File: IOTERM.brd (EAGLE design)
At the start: 135.9 x 53.3 mm, 45 parts

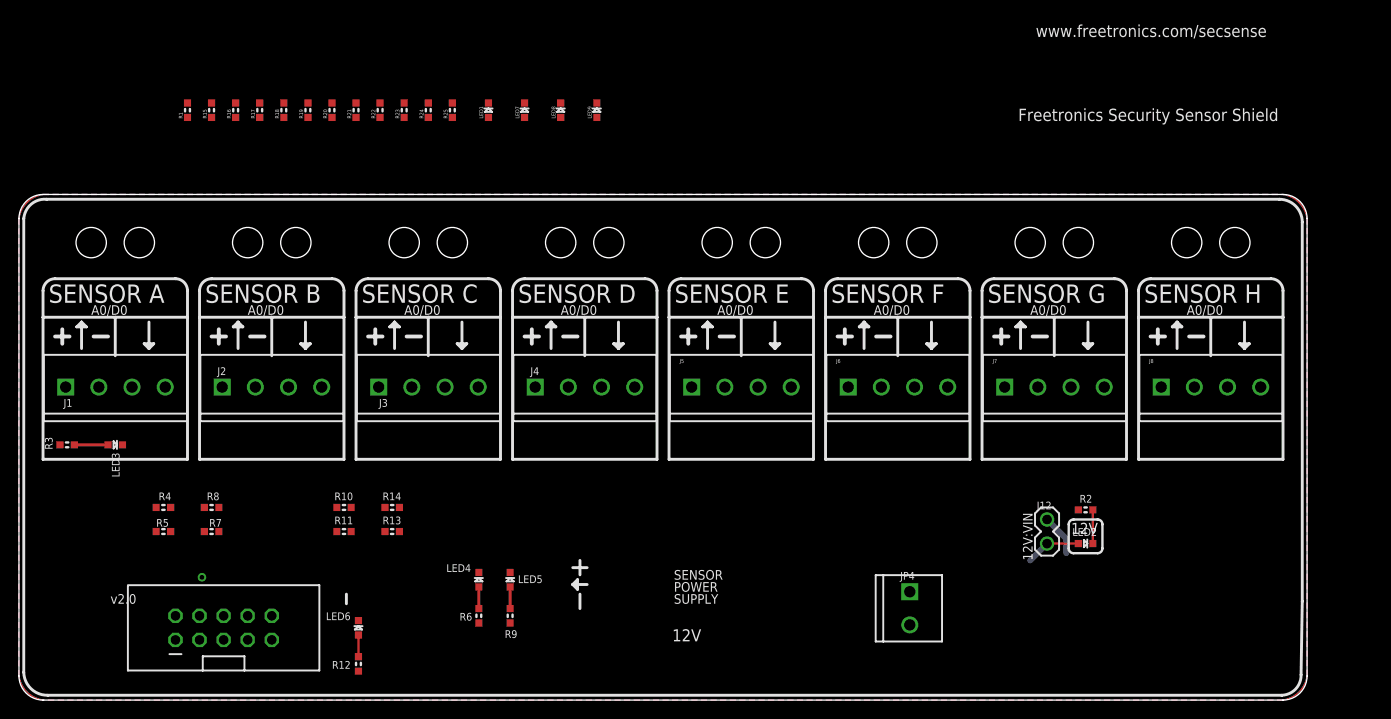
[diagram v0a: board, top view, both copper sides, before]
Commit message: Expanded header to 2x6 for v2.0 release
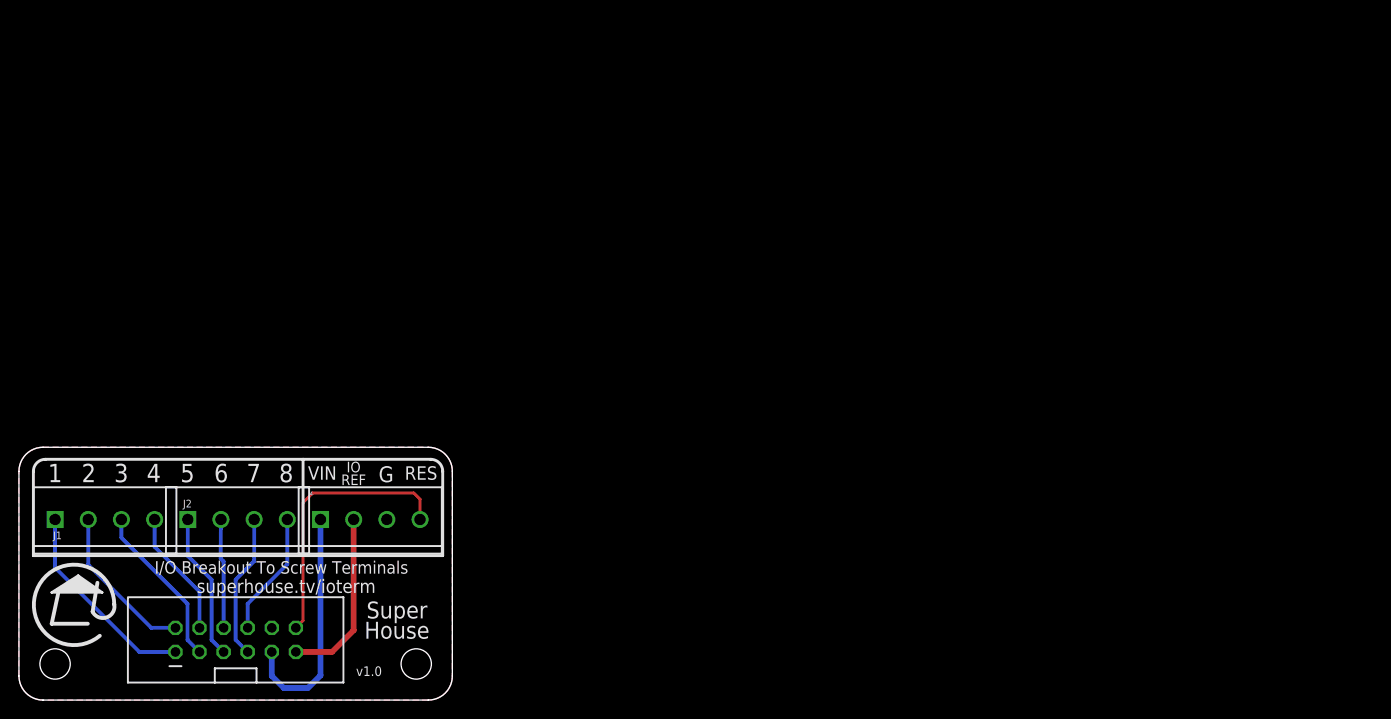
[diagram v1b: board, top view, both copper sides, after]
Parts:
- removed J12: (no value), freetronics-original:1X02
- removed J3, J5, J6, J7, J8: (no value), freetronics-master-v1.1:SCREWTERMINAL-3.5MM-4
- removed JP4: (no value), freetronics-master-v1.1:SCREWTERMINAL-3.5MM-2
- removed LED1, LED3, LED4, LED5, LED6, LED7, LED8, LED9: RED, freetronics-jon:LED-0603
- removed LED2: GREEN, freetronics-jon:LED-0603
- removed R1, R12, R15, R16, R17, R3, R6, R9: 560R, freetronics-jon:0603
- removed R10, R13, R18, R19, R20, R21, R4, R7: 4K7, freetronics-jon:0603
- removed R11, R14, R2, R22, R23, R24, R25, R5, R8: 1K, freetronics-jon:0603
- J1: value (none) -> D0_D3
- J2: value (none) -> D4_D7
- J4: value (none) -> Power
- JP1: value M05X2SHD -> M06X2; device freetronics-original:2X5-SHROUDED -> freetronics-jon:2X6-SHROUDED
- moved J4 26.6 mm to (31.8, 19.1)
- moved J2 14.4 mm to (17.8, 19.1)
- moved J1 14.0 mm to (3.81, 19.1)
- moved JP1 5.68 mm to (16.5, 5.08)
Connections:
- removed net 12V: J1.1, J12.1, J2.1, J3.1, J4.1, J5.1, J6.1, J7.1, J8.1, JP4.1, LED2.A
- removed net 5V: R10.1, R13.1, R18.1, R19.1, R20.1, R21.1, R4.1, R7.1
- removed net A0: R5.1
- removed net A1: R8.1
- removed net A2: R11.1
- removed net A3: R14.1
- removed net N$1: LED2.C, R2.2
- removed net N$10: J8.4, R21.2, R25.2
- removed net N$11: JP1.5
- removed net N$12: JP1.3
- removed net N$13: JP1.1
- removed net N$14: JP1.7
- removed net N$15: LED1.A, R1.1
- removed net N$16: LED7.A, R15.1
- removed net N$17: LED8.A, R16.1
- removed net N$18: LED9.A, R17.1
- removed net N$19: R1.2
- removed net N$2: R3.2
- removed net N$20: R15.2
- removed net N$21: R16.2
- removed net N$22: R17.2
- removed net N$23: R22.1
- removed net N$24: R23.1
- removed net N$249: J3.4, R10.2, R11.2
- removed net N$25: R24.1
- removed net N$251: LED6.A, R12.1
- removed net N$252: LED5.A, R9.1
- removed net N$253: LED4.A, R6.1
- removed net N$254: LED3.A, R3.1
- removed net N$256: J4.4, R13.2, R14.2
- removed net N$26: R25.1
- removed net N$262: J1.4, R4.2, R5.2
- removed net N$27: JP1.8
- removed net N$28: JP1.6
- removed net N$29: JP1.4
- removed net N$3: J2.4, R7.2, R8.2
- removed net N$30: JP1.2
- removed net N$4: R6.2
- removed net N$5: R9.2
- removed net N$6: R12.2
- removed net N$7: J5.4, R18.2, R22.2
- removed net N$8: J6.4, R19.2, R23.2
- removed net N$9: J7.4, R20.2, R24.2
- removed net VCC: JP1.9
- new net D0: J1.1, JP1.1
- new net D1: J1.2, JP1.2
- new net D2: J1.3, JP1.3
- new net D3: J1.4, JP1.4
- new net D4: J2.1, JP1.5
- new net D5: J2.2, JP1.6
- new net D6: J2.3, JP1.7
- new net D7: J2.4, JP1.8
- new net IOREF: J4.2, JP1.11
- new net RESET: J4.4, JP1.12
- net GND: no longer J1.2, J1.3, J2.2, J2.3, J3.2, J3.3, J4.2, J5.2, J5.3, J6.2, J6.3, J7.2, J7.3, J8.2, J8.3, JP4.2, LED1.C, LED3.C, LED4.C, LED5.C, LED6.C, LED7.C, LED8.C, LED9.C, R2.1
- net VIN: now also J4.1, JP1.9; no longer J12.2
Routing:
- net RESET: track 0.00 -> 28.7 mm
- net D0: track 0.00 -> 21.5 mm
- net VIN: track 4.40 -> 25.2 mm
- net IOREF: track 0.00 -> 18.7 mm
- net D2: track 0.00 -> 17.4 mm
- net D1: track 0.00 -> 16.7 mm
- net D4: track 0.00 -> 15.5 mm
- net D6: track 0.00 -> 15.3 mm
- net D3: track 0.00 -> 13.4 mm
- net D7: track 0.00 -> 13.2 mm
- net D5: track 0.00 -> 11.6 mm
- net 12V: track 5.82 -> 0.00 mm
- net N$254: track 3.56 -> 0.00 mm
- net N$1: track 3.56 -> 0.00 mm
- net N$253: track 2.29 -> 0.00 mm
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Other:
- board size 135.9 x 53.3 mm -> 45.7 x 26.7 mm
- board text added: "(c) 2017 SuperHouse Automation Pty Ltd"
- board text added: "1"
- board text added: "2"
- board text added: "3"
- board text added: "4"
- board text added: "5"
- board text added: "6"
- board text added: "7"
- board text added: "8"
- board text added: "G"
- board text added: "GND"
- board text added: "I/O Breakout To Screw Terminals"
- board text added: "IO REF"
- board text added: "IOREF"
- board text added: "RES"
- board text added: "RESET"
- board text added: "SKU: IOTERM"
- board text added: "Super House"
- board text added: "VIN"
- board text added: "superhouse.tv/ioterm"
- board text added: "v1.0"
- board text removed: "(c) 2013 Freetronics Pty Ltd"
- board text removed: "+12V"
- board text removed: "0V"
- board text removed: "12V"
- board text removed: "12V:VIN"
- board text removed: "4-Channel Security Sensor Shield"
- board text removed: "4K7"
- board text removed: "A"
- board text removed: "A0/D0"
- board text removed: "A: A0/D4 B: A1/D5 C: A2/D6 D: A3/D7"
- board text removed: "ALARM N.C."
- board text removed: "Freetronics Security Sensor Shield"
- board text removed: "K"
- board text removed: "POWER"
- board text removed: "SENSOR"
- board text removed: "SENSOR A"
- board text removed: "SENSOR B"
- board text removed: "SENSOR C"
- board text removed: "SENSOR D"
- board text removed: "SENSOR E"
- board text removed: "SENSOR F"
- board text removed: "SENSOR G"
- board text removed: "SENSOR H"
- board text removed: "SHIELD"
- board text removed: "SKU: SECSENSE"
- board text removed: "SUPPLY"
- board text removed: "TAMPER N.C."
- board text removed: "freetronics"
- board text removed: "v2.0"
- board text removed: "www.freetronics.com"
- board text removed: "www.freetronics.com/secsense"

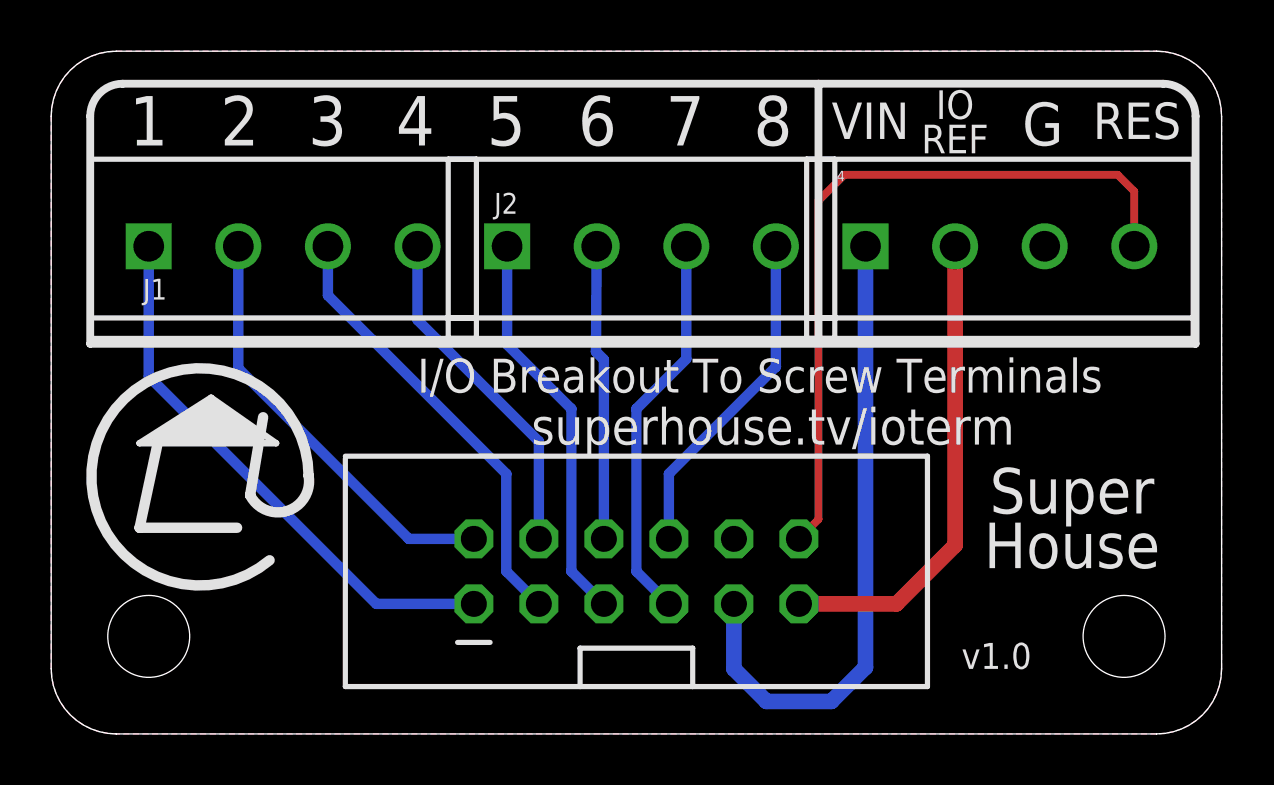
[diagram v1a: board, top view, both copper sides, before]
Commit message: Adjusted size to metric grid
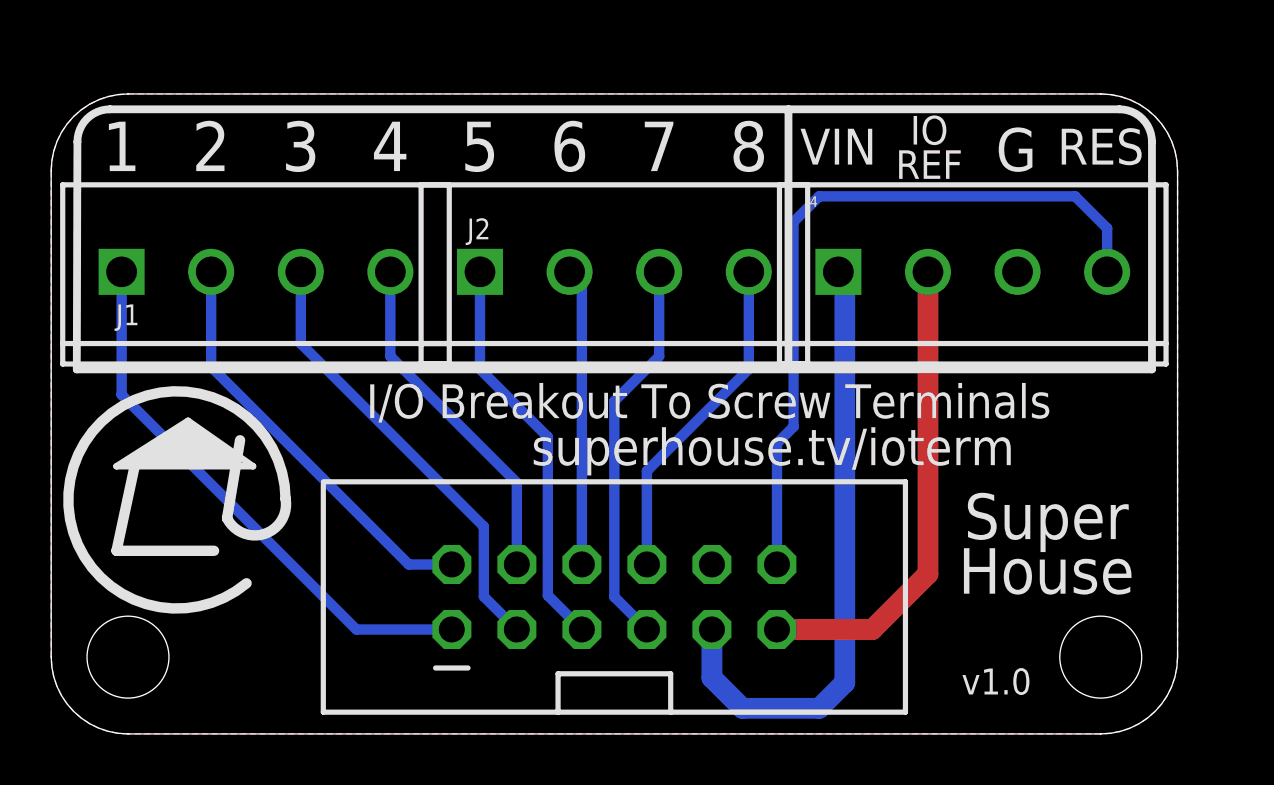
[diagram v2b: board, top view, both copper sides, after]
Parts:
- moved J1 1.46 mm to (2.75, 18.1)
- moved J2 1.46 mm to (16.8, 18.1)
- moved J4 1.46 mm to (30.8, 18.1)
- moved JP1 1.32 mm to (15.7, 4.08)
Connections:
- net D0 renamed IO1
- net D1 renamed IO2
- net D2 renamed IO3
- net D3 renamed IO4
- net D4 renamed IO5
- net D5 renamed IO6
- net D6 renamed IO7
- net D7 renamed IO8
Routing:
- net VIN: track 25.2 -> 24.1 mm
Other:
- board size 45.7 x 26.7 mm -> 44 x 25 mm
